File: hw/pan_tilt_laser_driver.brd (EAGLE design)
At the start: 38.1 x 20.3 mm, 37 parts, among them IC2 998-MIC5219-3.0YMM, IC3 FT2232H, IC5 93C46, IC6 998-MIC5219-3.0YMM, X1 798-ZX62RD-AB-5P8, X2 12MHz

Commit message: Outline replaced, in progress
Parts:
- removed C10, C11: 27pF, dp_devices:C805
- removed C13: 4.7uF, dp_devices:SMC_A
- removed C14, C15, C16, C17, C18, C19, C20, C21, C22, C9: 0.1uF, dp_devices:C805
- removed IC2, IC6: 998-MIC5219-3.0YMM, v-reg-micrel:MSOP08
- removed IC3: FT2232H, DP-EagleLibrary:LQFP64
- removed R7: 10k, dp_devices:R805
- removed X2: 12MHz, dp_devices:4X6
- added C1, C2, C31, C32: 0.1u, rcl:C0603K
- added C111, C56: C1608X5R1C106M080AB, SparkFun-Passives:0603-CAP
- added C123: VJ0603A471KXQPW1BC, SparkFun-Passives:0603-CAP
- added C28, C5: (no value), rcl:C0603K
- added C29, C30: 4.7u, rcl:C0603K
- added C90, C99: 18p, rcl:C0603K
- added J1: POWER_JACKPTH, SparkFun-Connectors:POWER_JACK_PTH
- added R1: 10k, rcl:R0603
- added U1: CAT6219-330TDGT3, SparkFun-PowerIC:SOT23-5
- added U2: (no value), torpedo:LQFP64
- added U3: LD3985M30R, SparkFun-PowerIC:SOT23-5
- added Y1: 405I35D12M00000, SparkFun-FreqCtrl:CRYSTAL-SMD-5X3
- C12: value 4.7uF -> 3.3u; device dp_devices:SMC_A -> rcl:C0603K
- C3: value C1608X5R1C106M080AB -> 0.1; device SparkFun-Passives:0603-CAP -> rcl:C0603K
- C4: value C1608X5R1C106M080AB -> (none); device SparkFun-Passives:0603-CAP -> rcl:C0603K
- C6: value VJ0603A471KXQPW1BC -> (none); device SparkFun-Passives:0603-CAP -> rcl:C0603K
- C8: value 3.3uF -> .1u; device dp_devices:SMC_A -> rcl:C0603K
- JP2: value 651-5442251 -> (none); device SparkFun-Connectors:SCREWTERMINAL-3.5MM-3 -> torpedo:22-03-5035
- L1, L2: value (none) -> BLM21PG331SN1D
- R2, R3, R4, R5, R6: device dp_devices:R805 -> rcl:R0603
- moved R4 135.7 mm to (-41.9, -160.0)
- moved R3 118.9 mm to (-12.3, -94.9), turned to 0 degrees
- moved JP2 100.1 mm to (49.5, 30.5)
- moved R2 95.3 mm to (-12.3, -109.3)
- moved IC5 85.7 mm to (90.9, 11.0), turned to 180 degrees
- moved C6 83.0 mm to (-12.3, -70.2)
- moved C8 79.4 mm to (-12.3, -118.0)
- moved C12 77.2 mm to (-12.3, -113.8)
- moved C4 76.8 mm to (-12.3, -64.1), turned to 0 degrees
- moved R5 75.2 mm to (-12.3, -99.7)
- moved X1 73.2 mm to (74.0, 14.0), turned to 90 degrees
- moved C3 73.2 mm to (-12.3, -61.1), turned to 0 degrees
- moved R6 62.7 mm to (-12.3, -104.5)
- moved JP1 44.1 mm to (68.6, 30.5), turned to 180 degrees
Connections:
- removed net !SUSPEND: IC3.36
- removed net +3V3: C24.1, IC6.3
- removed net N$2: C6.1, IC2.4
- removed net PAN_TILT_RXD: IC3.39, JP2.1
- new net N$8: C25.1, U1.4
- new net SERVO_POWER: J1.PWR, JP2.2
- net !RESET: now also R6.1, U2.14; no longer IC3.14, R3.2
- net 1.8V: now also C1.1, C12.1, C2.1, C3.1, U2.12, U2.37, U2.49, U2.64; no longer C16.1, C17.1, C18.1, C8.+, IC3.12, IC3.37, IC3.49, IC3.64
- net 3.3V: now also C24.1, C28.1, C4.1, C5.1, C6.1, C8.1, R1.2, R3.2, U1.5, U2.20, U2.31, U2.42, U2.50, U2.56; no longer C19.1, C20.1, C21.1, C22.1, C9.1, IC3.20, IC3.31, IC3.42, IC3.50, IC3.56, R3.1, R7.2
- net 5V: now also C56.1, U1.1, U1.3, U3.1; no longer C3.1, IC2.2, IC6.1, IC6.2
- net EECLK: now also R5.1, U2.62; no longer IC3.62, R7.1
- net EECS: now also R3.1, U2.63; no longer IC3.63, R6.1
- net EEDATA: now also R4.1, U2.61; no longer IC3.61, R4.2
- net GND: now also C1.2, C111.2, C12.2, C123.2, C2.2, C28.2, C29.2, C30.2, C31.2, C32.2, C5.2, C56.2, C8.2, C90.1, C99.1, J1.GND, J1.GNDBREAK, JP2.1, R2.2, U1.2, U2.1, U2.10, U2.11, U2.13, U2.15, U2.25, U2.35, U2.47, U2.5, U2.51, U3.2; no longer C10.1, C11.1, C12.-, C13.-, C14.2, C15.2, C16.2, C17.2, C18.2, C19.2, C20.2, C21.2, C22.2, C8.-, C9.2, IC2.5, IC2.6, IC2.7, IC2.8, IC3.1, IC3.10, IC3.11, IC3.13, IC3.15, IC3.25, IC3.35, IC3.47, IC3.5, IC3.51, IC3.60, IC6.5, IC6.6, IC6.7, IC6.8, JP2.3, R2.1
- net LASER_EN: now also U2.21, U3.3; no longer IC2.1, IC3.18
- net LASER_PWR: now also C111.1, U3.5; no longer C4.1, IC2.3
- net LASER_TXD: now also U2.16; no longer IC3.16
- net N$1: now also C123.1, U3.4; no longer C25.1, IC6.4
- net N$10: now also C90.2, U2.3, Y1.1; no longer C11.2, IC3.3, X2.1
- net N$3: now also U2.7; no longer IC3.7
- net N$4: now also R2.1, U2.6; no longer IC3.6, R2.2
- net N$45: now also R1.1, R4.2; no longer R4.1, R5.1
- net N$5: now also U2.8; no longer IC3.8
- net N$6: now also C29.1, C31.1, U2.9; no longer C12.+, C14.1, IC3.9
- net N$7: now also C99.2, U2.2, Y1.3; no longer C10.2, IC3.2, X2.2
- net N$9: now also C30.1, C32.1, U2.4; no longer C13.+, C15.1, IC3.4
- net PAN_TILT_TXD: now also JP2.3, U2.38; no longer IC3.38, JP2.2
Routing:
- removed copper zone on layer 1, net GND
- removed copper zone on layer 16, net GND
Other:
- board size 38.1 x 20.3 mm -> 76.2 x 34.2 mm

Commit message: Preliminary placement complete.
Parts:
- removed C111, C23, C24, C56: C1608X5R1C106M080AB, SparkFun-Passives:0603-CAP
- removed C123, C25: VJ0603A471KXQPW1BC, SparkFun-Passives:0603-CAP
- removed C28: (no value), rcl:C0603K
- removed C29, C30: 4.7u, rcl:C0603K
- removed C31, C32: 0.1u, rcl:C0603K
- removed C90, C99: 18p, rcl:C0603K
- removed IC5: 93C46, dp_devices:SOIC8
- added C10, C11: VJ0603A471KXQPW1BC, SparkFun-Passives:0603-CAP
- added C13, C14: C1608X5R1C106M080AB, SparkFun-Passives:0603-CAP
- added C15, C16: 18p, rcl:C0603K
- added C17, C19: 4.7u, rcl:C0603K
- added C18: 3.3u, rcl:C0603K
- added C20, C21: 0.1u, rcl:C0603K
- added C7, C9: (no value), rcl:C0603K
- added IC1: 93C46, dp_devices:SOIC8
- C12: value 3.3u -> .1u
- C4, C5: value (none) -> C1608X5R1C106M080AB; device rcl:C0603K -> SparkFun-Passives:0603-CAP
- C8: value .1u -> (none)
- JP1: value 651-5442251 -> (none); device SparkFun-Connectors:SCREWTERMINAL-3.5MM-3 -> torpedo:22-03-5035
- JP2: value (none) -> 651-5442251; device torpedo:22-03-5035 -> SparkFun-Connectors:SCREWTERMINAL-3.5MM-3
- R2: value 12k 1% -> 2.2k
- R4: value 2.2k -> 10k
- R5: value 10k -> 12k 1%
- U2: value (none) -> LD3985M30R; device torpedo:LQFP64 -> SparkFun-PowerIC:SOT23-5
- U3: value LD3985M30R -> (none); device SparkFun-PowerIC:SOT23-5 -> torpedo:LQFP64
- moved U1 188.6 mm to (64.3, 31.5)
- moved R4 182.3 mm to (34.8, 5.33), turned to 270 degrees
- moved U2 176.7 mm to (16.8, 17.3), turned to 90 degrees
- moved U3 174.0 mm to (45.7, 17.3), turned to 180 degrees
- moved C8 155.3 mm to (48.0, 25.1), turned to 90 degrees
- moved R5 140.1 mm to (53.5, 24.0)
- moved C12 131.5 mm to (27.3, 11.6)
- moved R2 128.5 mm to (34.8, 10.2), turned to 90 degrees
- moved R6 120.5 mm to (37.1, 5.33), turned to 270 degrees
- moved C4 120.2 mm to (64.3, 28.4)
- moved R1 109.8 mm to (32.5, 10.2), turned to 90 degrees
- moved R3 109.8 mm to (32.5, 5.33), turned to 270 degrees
- moved C3 104.1 mm to (52.7, 20.2), turned to 90 degrees
- moved C6 100.2 mm to (37.8, 16.5), turned to 180 degrees
- moved C2 92.0 mm to (37.8, 19.1), turned to 180 degrees
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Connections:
- net !RESET: now also U3.14; no longer U2.14
- net 1.8V: now also C18.1, U3.12, U3.37, U3.49, U3.64; no longer C12.1, U2.12, U2.37, U2.49, U2.64
- net 3.3V: now also C12.1, C13.1, C7.1, C9.1, IC1.6, IC1.8, R4.2, U3.20, U3.31, U3.42, U3.50, U3.56; no longer C24.1, C28.1, C4.1, C5.1, IC5.6, IC5.8, R5.2, U2.20, U2.31, U2.42, U2.50, U2.56
- net 5V: now also C4.1, C5.1, U2.1; no longer C23.1, C56.1, U3.1
- net EECLK: now also IC1.2, R4.1, U3.62; no longer IC5.2, R5.1, U2.62
- net EECS: now also IC1.1, U3.63; no longer IC5.1, U2.63
- net EEDATA: now also IC1.3, R2.1, U3.61; no longer IC5.3, R4.1, U2.61
- net GND: now also C10.2, C11.2, C13.2, C14.2, C15.1, C16.1, C17.2, C18.2, C19.2, C20.2, C21.2, C7.2, C9.2, IC1.5, JP1.1, JP2.3, R5.2, U2.2, U3.1, U3.10, U3.11, U3.13, U3.15, U3.25, U3.35, U3.47, U3.5, U3.51; no longer C111.2, C123.2, C23.2, C24.2, C25.2, C28.2, C29.2, C30.2, C31.2, C32.2, C56.2, C90.1, C99.1, IC5.5, JP1.3, JP2.1, R2.2, U2.1, U2.10, U2.11, U2.13, U2.15, U2.25, U2.35, U2.47, U2.5, U2.51, U3.2
- net LASER_EN: now also U2.3, U3.21; no longer U2.21, U3.3
- net LASER_PWR: now also C14.1, JP2.1, U2.5; no longer C111.1, JP1.1, U3.5
- net LASER_TXD: now also JP2.2, U3.16; no longer JP1.2, U2.16
- net N$1: now also C11.1, U2.4; no longer C123.1, U3.4
- net N$10: now also C16.2, U3.3; no longer C90.2, U2.3
- net N$3: now also U3.7; no longer U2.7
- net N$4: now also R5.1, U3.6; no longer R2.1, U2.6
- net N$45: now also IC1.4, R2.2; no longer IC5.4, R4.2
- net N$5: now also U3.8; no longer U2.8
- net N$6: now also C17.1, C20.1, U3.9; no longer C29.1, C31.1, U2.9
- net N$7: now also C15.2, U3.2; no longer C99.2, U2.2
- net N$8: now also C10.1; no longer C25.1
- net N$9: now also C19.1, C21.1, U3.4; no longer C30.1, C32.1, U2.4
- net PAN_TILT_TXD: now also JP1.3, U3.38; no longer JP2.3, U2.38
- net SERVO_POWER: now also JP1.2; no longer JP2.2
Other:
- board size 76.2 x 34.2 mm -> 76.7 x 34.2 mm

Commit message: Rough Signal Routing
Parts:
- moved R6 24.9 mm to (53.3, 24.1), turned to 90 degrees
- moved R5 10.8 mm to (58.3, 14.4), turned to 270 degrees
- moved C16 3.31 mm to (56.9, 9.65), turned to 90 degrees
- moved C15 3.06 mm to (56.9, 6.60), turned to 270 degrees
- moved R1 2.30 mm to (34.8, 10.4)
- moved R2 2.30 mm to (32.5, 10.4)
- moved R3 2.29 mm to (34.8, 5.33)
- moved R4 2.29 mm to (32.5, 5.33)
- moved C2 0.57 mm to (37.3, 19.3)
- moved C17 0.51 mm to (55.8, 19.7)
- moved C20 0.51 mm to (55.8, 21.0)
- moved L1 0.51 mm to (55.8, 18.0)
- moved C3 0.25 mm to (52.7, 19.9)
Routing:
- net LASER_TXD: track 0.00 -> 44.4 mm
- net LASER_EN: track 0.00 -> 40.6 mm
- net EECS: track 0.00 -> 25.5 mm
- net EECLK: track 0.00 -> 24.8 mm
- net EEDATA: track 0.00 -> 23.3 mm
- net N$5: track 0.00 -> 22.9 mm
- net N$3: track 0.00 -> 22.8 mm
- net N$7: track 0.00 -> 16.8 mm
- net N$10: track 0.00 -> 15.8 mm
- net 1.8V: track 0.00 -> 15.5 mm
- net PAN_TILT_TXD: track 0.00 -> 15.5 mm
- net LASER_PWR: track 0.00 -> 12.4 mm
- net N$4: track 0.00 -> 7.31 mm
- net N$6: track 0.00 -> 6.73 mm
- net N$45: track 0.00 -> 6.06 mm
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
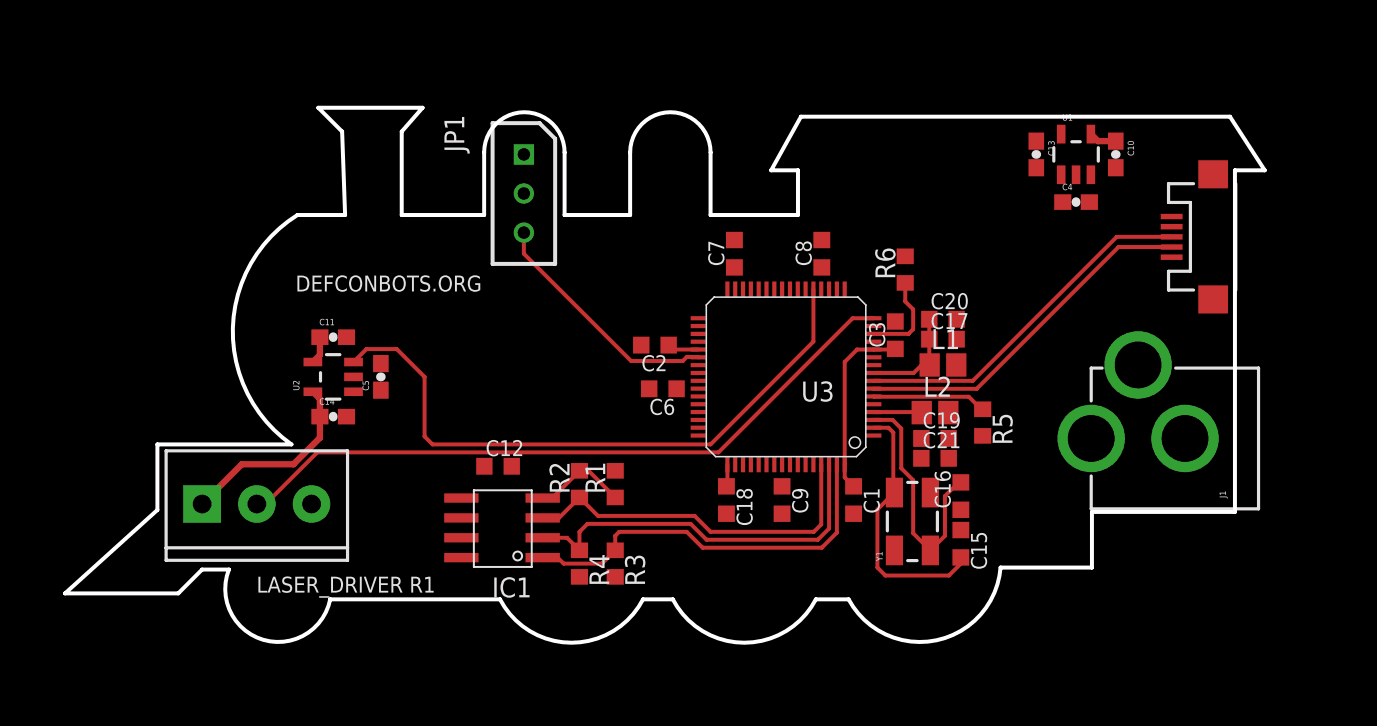
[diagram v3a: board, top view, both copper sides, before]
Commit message: Finished initial routing.
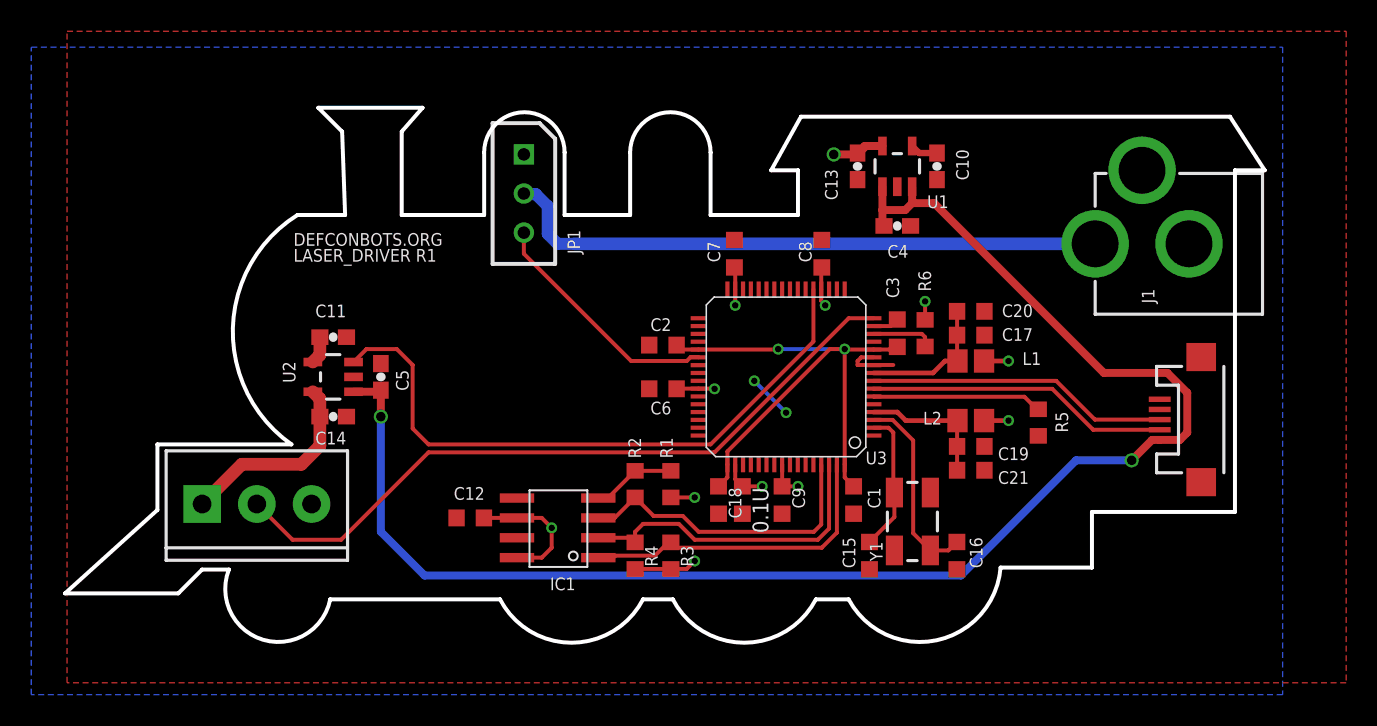
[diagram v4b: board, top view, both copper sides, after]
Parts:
- added 0.1U: (no value), rcl:C0603K
- moved J1 12.4 mm to (79.2, 25.8)
- moved X1 11.7 mm to (72.3, 14.5)
- moved C4 11.5 mm to (52.8, 26.9)
- moved C10 11.5 mm to (55.4, 30.7)
- moved C13 11.5 mm to (50.3, 30.7)
- moved U1 11.5 mm to (52.8, 30.7)
- moved C15 5.89 mm to (51.1, 5.84), turned to 90 degrees
- moved R6 4.26 mm to (54.6, 20.1)
- moved C16 3.82 mm to (56.6, 5.84)
- moved C12 3.75 mm to (25.5, 8.26), turned to 180 degrees
- moved R3 3.59 mm to (38.4, 5.84)
- moved R4 3.59 mm to (36.1, 5.84)
- moved IC1 3.56 mm to (31.1, 7.62)
- moved R1 3.56 mm to (38.4, 10.4), turned to 270 degrees
- moved R2 3.56 mm to (36.1, 10.4)
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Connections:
- net 3.3V: now also 0.1U.1
- net GND: now also 0.1U.2
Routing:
- net 5V: track 0.00 -> 98.2 mm, vias 0 -> 2
- net SERVO_POWER: track 0.00 -> 38.9 mm
- net 3.3V: track 0.00 -> 36.0 mm, vias 0 -> 12
- net 1.8V: track 15.5 -> 36.5 mm, vias 0 -> 2
- net GND: track 0.00 -> 8.22 mm, vias 0 -> 2
- net N$7: track 16.8 -> 9.07 mm
- net N$9: track 3.09 -> 8.77 mm
- net EECS: track 25.5 -> 20.6 mm
- net EECLK: track 24.8 -> 20.6 mm
- net EEDATA: track 23.3 -> 19.7 mm
- net N$4: track 7.31 -> 10.9 mm
- net N$5: track 22.9 -> 19.3 mm
- net N$3: track 22.8 -> 19.4 mm
- net N$10: track 15.8 -> 12.5 mm
- net N$6: track 6.73 -> 9.31 mm
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- added copper zone on layer 16, net 3.3V
- added copper zone on layer 1, net GND

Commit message: Final version of the ref hw.
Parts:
- added LED1, LED2: (no value), SparkFun-LED:LED-1206
- added R7, R8: 330, rcl:R0603
- C10, C11: value VJ0603A471KXQPW1BC -> 0.01u
- C12: value .1u -> 0.1u
- C13, C14, C4, C5: value C1608X5R1C106M080AB -> 10u
- C18: value 3.3u -> 10u
- C22, C6, C7, C8, C9: value (none) -> 0.1u
- C3: value 0.1 -> 0.1u
- renumbered 0.1U to C22
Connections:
- new net N$11: LED2.A, R8.2
- new net N$2: LED1.A, R7.2
- net 3.3V: now also R8.1
- net GND: now also LED1.C, LED2.C
- net SERVO_POWER: now also R7.1
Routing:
- net SERVO_POWER: track 38.9 -> 46.3 mm
- net N$2: track 0.00 -> 2.30 mm
- net N$11: track 0.00 -> 2.30 mm
- net 3.3V: track 36.0 -> 38.0 mm, vias 12 -> 13

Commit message: Fix part number for USB micro connector (was wrong direction part -- upside down).
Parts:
- X1: value 798-ZX62RD-AB-5P8 -> 538-47346-0001
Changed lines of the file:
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@@
 </autorouter>
 <elements>
-<element name="X1" library="SparkFun" package="USB-MICROB" value="798-ZX62RD-AB-5P8" x="72.263" y="14.5415" smashed="yes" rot="R90">
+<element name="X1" library="SparkFun" package="USB-MICROB" value="538-47346-0001" x="72.263" y="14.5415" smashed="yes" rot="R90">
 <attribute name="VALUE" x="75.438" y="12.6365" size="0.8128" layer="27" font="vector" ratio="12" rot="R90"/>
 </element>

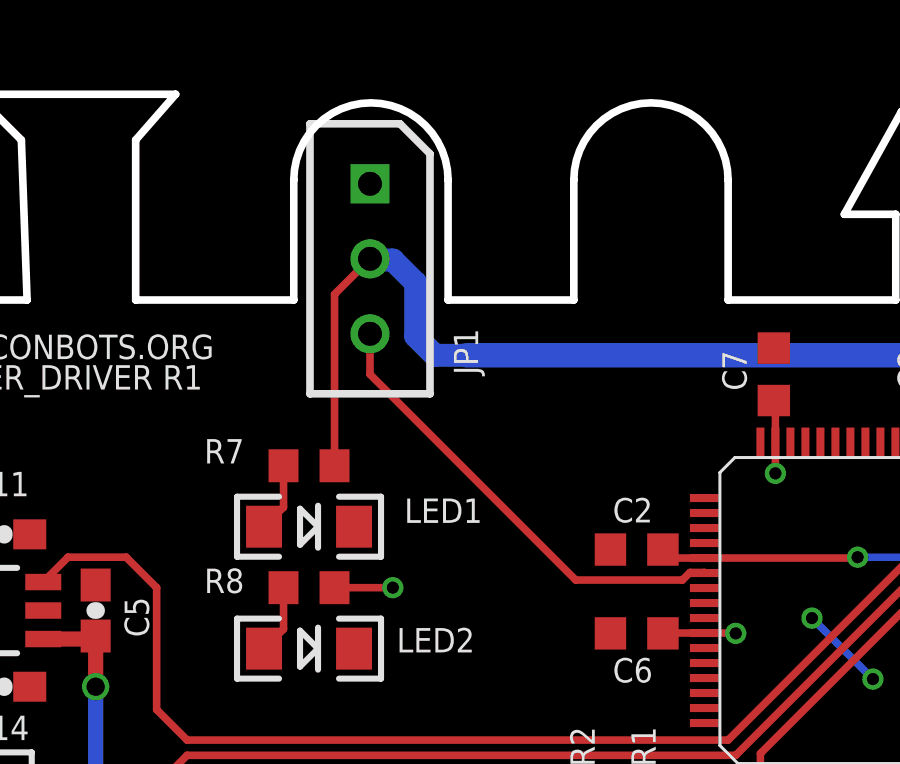
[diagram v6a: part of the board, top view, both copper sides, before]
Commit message: Servo connector was backwards. Fixed in schematic and layout.
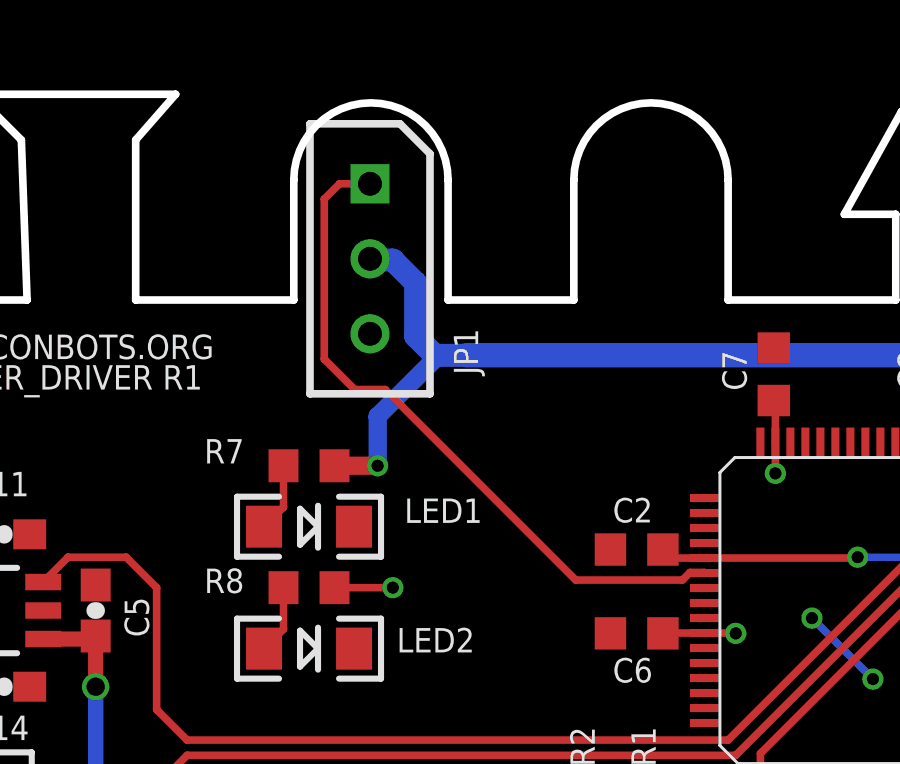
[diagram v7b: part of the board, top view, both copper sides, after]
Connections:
- net GND: now also JP1.3; no longer JP1.1
- net PAN_TILT_TXD: now also JP1.1; no longer JP1.3
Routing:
- net PAN_TILT_TXD: track 15.5 -> 22.9 mm
- net SERVO_POWER: track 46.3 -> 44.9 mm, vias 0 -> 1
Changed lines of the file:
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@@
 <contactref element="C14" pad="2"/>
 <contactref element="U3" pad="13"/>
-<contactref element="JP1" pad="1"/>
 <contactref element="U3" pad="1"/>
 <contactref element="U3" pad="51"/>
@@
 <contactref element="LED1" pad="C"/>
 <contactref element="LED2" pad="C"/>
+<contactref element="JP1" pad="3"/>
 </signal>
 <signal name="3.3V" class="1">
@@
 </signal>
 <signal name="PAN_TILT_TXD">
-<contactref element="JP1" pad="3"/>
 <contactref element="U3" pad="38"/>
 <wire x1="40.12" y1="18.522" x2="40.1" y2="18.542" width="0.254" layer="1"/>
@@
 <wire x1="39.624" y1="18.542" x2="39.37" y2="18.288" width="0.254" layer="1"/>
 <wire x1="39.37" y1="18.288" x2="35.814" y2="18.288" width="0.254" layer="1"/>
-<wire x1="35.814" y1="18.288" x2="28.956" y2="25.146" width="0.254" layer="1"/>
-<wire x1="28.956" y1="25.146" x2="28.956" y2="26.496" width="0.254" layer="1"/>
+<wire x1="35.814" y1="18.288" x2="29.464" y2="24.638" width="0.254" layer="1"/>
+<contactref element="JP1" pad="1"/>
+<wire x1="29.464" y1="24.638" x2="28.448" y2="24.638" width="0.254" layer="1"/>
+<wire x1="28.448" y1="24.638" x2="27.432" y2="25.654" width="0.254" layer="1"/>
+<wire x1="27.432" y1="25.654" x2="27.432" y2="30.988" width="0.254" layer="1"/>
+<wire x1="27.432" y1="30.988" x2="27.94" y2="31.496" width="0.254" layer="1"/>
+<wire x1="27.94" y1="31.496" x2="28.956" y2="31.496" width="0.254" layer="1"/>
 </signal>
 <signal name="N$9">
@@
 <signal name="SERVO_POWER">
 <contactref element="J1" pad="PWR"/>
-<contactref element="JP1" pad="2"/>
 <wire x1="65.4845" y1="25.781" x2="32.171" y2="25.781" width="0.8128" layer="16"/>
-<wire x1="32.171" y1="25.781" x2="31.115" y2="25.781" width="0.762" layer="16"/>
+<wire x1="32.171" y1="25.781" x2="31.242" y2="25.781" width="0.762" layer="16"/>
+<wire x1="31.242" y1="25.781" x2="31.115" y2="25.781" width="0.762" layer="16"/>
 <wire x1="31.115" y1="25.781" x2="30.48" y2="26.416" width="0.762" layer="16"/>
 <wire x1="30.48" y1="26.416" x2="30.48" y2="28.194" width="0.762" layer="16"/>
 <wire x1="30.48" y1="28.194" x2="29.718" y2="28.956" width="0.762" layer="16"/>
 <wire x1="29.718" y1="28.956" x2="28.996" y2="28.956" width="0.762" layer="16"/>
-<wire x1="28.996" y1="28.956" x2="28.956" y2="28.996" width="0.762" layer="16"/>
 <contactref element="R7" pad="1"/>
-<wire x1="27.774" y1="22.098" x2="27.774" y2="27.814" width="0.254" layer="1"/>
-<wire x1="27.774" y1="27.814" x2="28.956" y2="28.996" width="0.254" layer="1"/>
+<contactref element="JP1" pad="2"/>
+<wire x1="28.996" y1="28.956" x2="28.956" y2="28.956" width="0.4064" layer="16"/>
+<wire x1="28.956" y1="28.956" x2="28.956" y2="28.996" width="0.4064" layer="16"/>
+<wire x1="27.774" y1="22.098" x2="29.21" y2="22.098" width="0.6096" layer="1"/>
+<via x="29.21" y="22.098" extent="1-16" drill="0.4064"/>
+<wire x1="29.21" y1="22.098" x2="29.21" y2="23.749" width="0.6096" layer="16"/>
+<wire x1="29.21" y1="23.749" x2="31.242" y2="25.781" width="0.6096" layer="16"/>
 </signal>
 <signal name="N$8">
